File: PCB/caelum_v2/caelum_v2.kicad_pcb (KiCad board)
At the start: 2 copper layers, 69 x 40.5 mm, 36 parts, among them J1 SS445P, J2 i2C Bus2, J3 Pulse1, J4 Batt, J7 I2C BUS1, J8 DS18B20, Q1 FS8205A-FC, U1 DW01A, U2 MCP1825S, U3 ESP32-H2-SUPERMINI

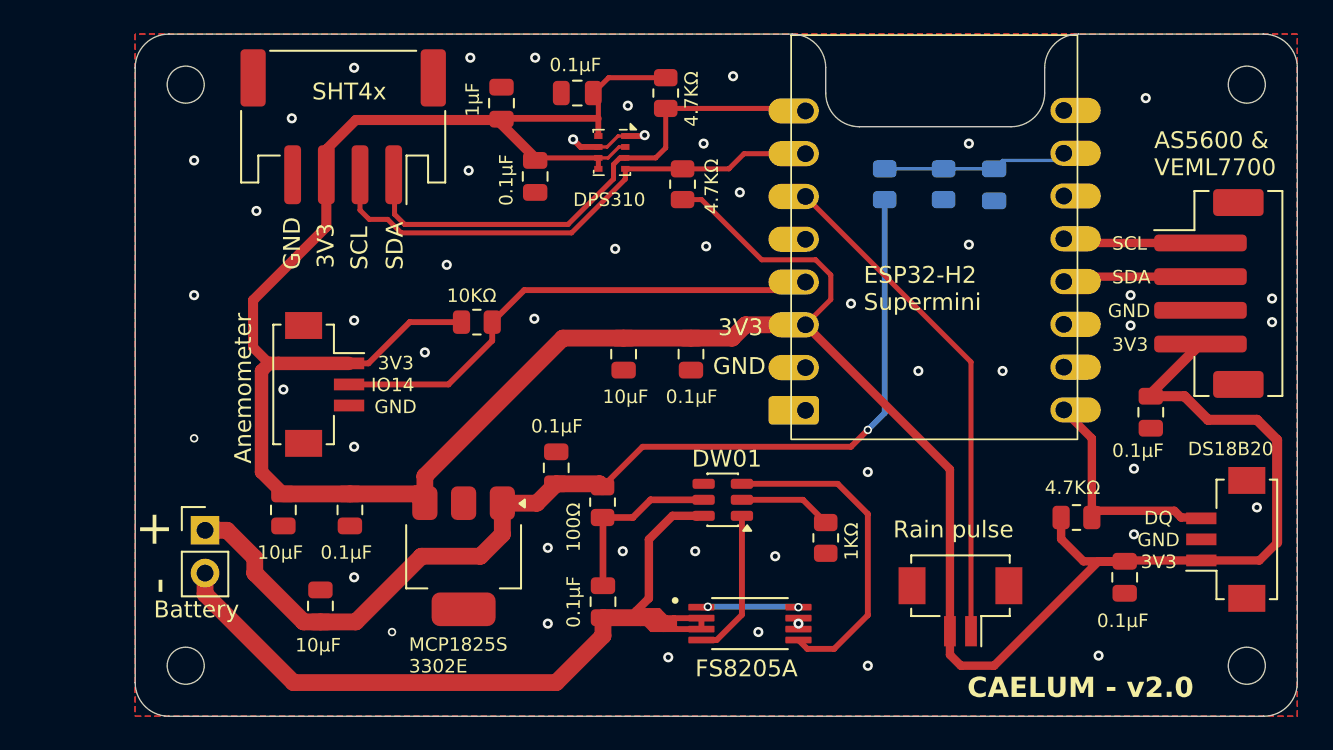
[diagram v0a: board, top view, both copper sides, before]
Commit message: Clone of Caelum v1
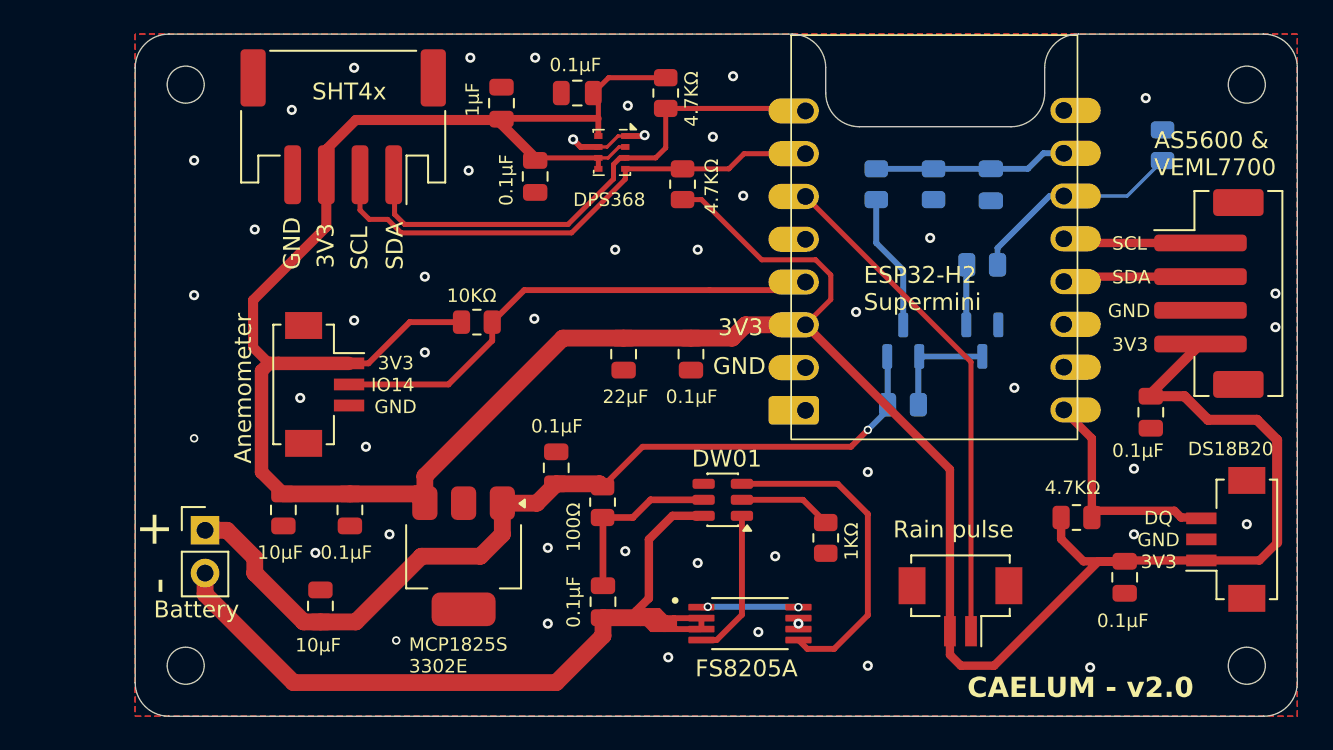
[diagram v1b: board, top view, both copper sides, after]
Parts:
- added Q2: BSS138, Package_TO_SOT_SMD:SOT-23, B.Cu at (96.3, 43.7)
- added Q3: Si2323DS, Package_TO_SOT_SMD:SOT-23, B.Cu at (91.6, 43.7)
- added R10: 100K, Resistor_SMD:R_0805_2012Metric, B.Cu at (107.0, 32.1)
- added R11: 100, Resistor_SMD:R_0805_2012Metric, B.Cu at (96.3, 39.2)
- added R9: 100K, Resistor_SMD:R_0805_2012Metric, B.Cu at (91.6, 47.5)
- R4: value 100K -> 10K
- R5: value 100K -> 22K
- moved R5 0.60 mm to (93.4, 34.4)
- moved R4 0.50 mm to (90.0, 34.4)
- moved C9 0.20 mm to (96.8, 34.5)
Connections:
- R4 pad 2: BATT+ -> Net-(Q3-D)
- U3 pad 14: unconnected-(U3-IO3-Pad14) -> GPIO3
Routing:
- net GPIO3: track 0.00 -> 12.9 mm
- net BATT+: track 62.2 -> 52.9 mm
- net Net-(Q3-D): track 0.00 -> 8.11 mm
- net Net-(Q2-D): track 0.00 -> 6.60 mm
- net Net-(Q2-G): track 0.00 -> 3.57 mm
- net GPIO4: track 11.0 -> 12.1 mm
- net OUT-: vias 49 -> 46
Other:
- board text added: "220KΩ"
- board text added: "22KΩ"
- board text added: "22µF"
- board text added: "BSS138"
- board text added: "DPS368"
- board text added: "Si2323"
- board text removed: "DPS310"

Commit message: Add ESP32 symbol and wind vane macro; update library paths
- Updated the library path for "caelum_v2" in fp-lib-table.
- Added ESP32 symbol to sym-lib-table for better component management.
- Created a new FreeCAD macro for generating a wind vane assembly compatible with the AS5600 sensor, including detailed parameters and assembly instructions.
- Introduced various components such as the rotating shaft, magnet holder, wind vane, arrow pointer, counterweight, central body, base mount, and sensor mount area.
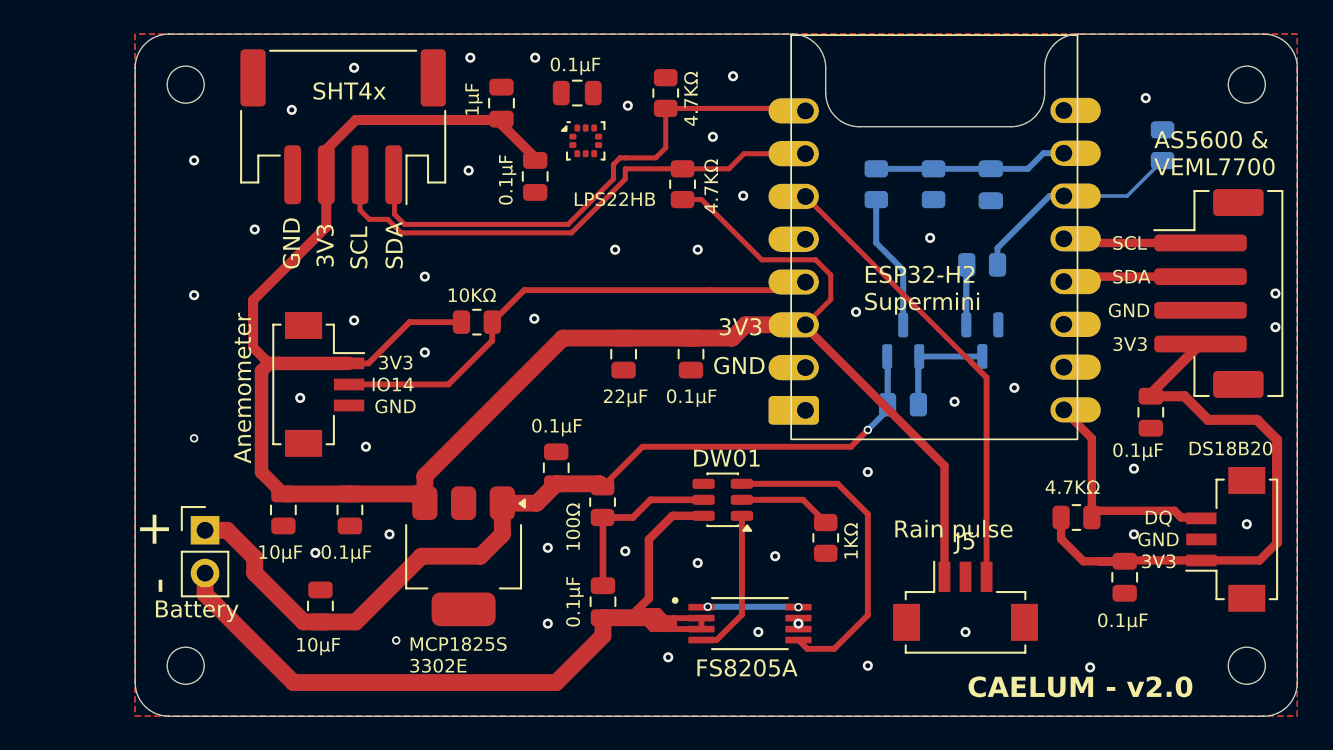
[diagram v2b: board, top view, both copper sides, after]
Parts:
- removed J3: Pulse1, Connector_Hirose:Hirose_DF13C_CL535-0402-2-51_1x02-1MP_P1.25mm_Vertical
- removed U4: ~, Package_LGA:Bosch_LGA-8_2x2.5mm_P0.65mm_ClockwisePinNumbering
- added J5: DRV5032DULPG(M), Connector_Hirose:Hirose_DF13C_CL535-0403-5-51_1x03-1MP_P1.25mm_Vertical, F.Cu at (95.3, 59.2)
- added U5: LPS22HB, Package_LGA:ST_HLGA-10_2x2mm_P0.5mm_LayoutBorder3x2y, F.Cu at (72.8, 31.8)
- C6: value 10µF -> 22µF
- R10: value 100K -> 220K-470K
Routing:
- net +3V3: track 191.1 -> 155.1 mm
- net OUT-: track 5.30 -> 0.57 mm
- net GPIO12: track 29.9 -> 27.0 mm
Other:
- board text added: "LPS22HB"
- board text removed: "DPS368"

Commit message: Refactor code structure for improved readability and maintainability
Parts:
- removed C12: 0.1µF, Capacitor_SMD:C_0805_2012Metric
- J1, J5, J8: footprint Connector_Hirose:Hirose_DF13C_CL535-0403-5-51_1x03-1MP_P1.25mm_Vertical -> Connector_JST:JST_PH_B3B-PH-SM4-TB_1x03-1MP_P2.00mm_Vertical
- J2: footprint Connector_JST:JST_PH_B4B-PH-SM4-TB_1x04-1MP_P2.00mm_Vertical -> Connector_JST:JST_PH_S4B-PH-SM4-TB_1x04-1MP_P2.00mm_Horizontal
- J4: footprint Connector_PinHeader_2.54mm:PinHeader_1x02_P2.54mm_Vertical -> Connector_JST:JST_PH_S2B-PH-SM4-TB_1x02-1MP_P2.00mm_Horizontal
- moved R8 6.03 mm to (71.7, 40.0)
- moved H1 6.00 mm to (43.0, 28.5)
- moved H2 6.00 mm to (43.0, 63.0)
- moved U5 5.67 mm to (75.2, 37.0)
- moved J4 5.35 mm to (45.0, 53.5), turned to 180 degrees
- moved J1 4.40 mm to (61.5, 45.0), turned to 90 degrees
- moved C10 3.56 mm to (72.0, 32.5), turned to 90 degrees
- moved C11 3.15 mm to (68.7, 32.6), turned to 90 degrees
- moved J2 1.91 mm to (109.5, 39.0), turned to 90 degrees
- moved J8 1.54 mm to (109.7, 54.4), turned to -90 degrees
- moved J5 0.22 mm to (95.5, 59.0), turned to 180 degrees
- moved J7 0.10 mm to (58.4, 31.1)
- turned C13 to 90 degrees
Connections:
- C13 pad 1: +3V3 -> OUT-
- C13 pad 2: OUT- -> +3V3
- J1 pad 1: +3V3 -> GPIO14
- J1 pad 2: GPIO14 -> OUT-
- J1 pad 3: OUT- -> +3V3
- J1 pad MP: (no net) -> OUT-
- J2 pad 1: SCL_2 -> OUT-
- J2 pad 2: SDA_2 -> +3V3
- J2 pad 3: OUT- -> SDA_2
- J2 pad 4: +3V3 -> SCL_2
- J2 pad MP: (no net) -> OUT-
- J5 pad 1: +3V3 -> GPIO13
- J5 pad 3: GPIO12 -> +3V3
- J5 pad MP: (no net) -> OUT-
- J7 pad 1: SDA -> OUT-
- J7 pad 2: SCL -> +3V3
- J7 pad 3: +3V3 -> SDA
- J7 pad 4: OUT- -> SCL
- J7 pad MP: (no net) -> OUT-
- J8 pad 1: +3V3 -> GPIO24
- J8 pad 3: GPIO24 -> +3V3
- J8 pad MP: (no net) -> OUT-
- U3 pad 5: unconnected-(U3-IO13-Pad5) -> GPIO13
- U5 pad 1: unconnected-(U5-Vdd_IO-Pad1) -> +3V3
- U5 pad 10: unconnected-(U5-VDD-Pad10) -> +3V3
- U5 pad 2: unconnected-(U5-SCL-Pad2) -> SCL
- U5 pad 3: Net-(U5-GND-Pad3) -> OUT-
- U5 pad 4: unconnected-(U5-SDA-Pad4) -> SDA
- U5 pad 5: unconnected-(U5-SA0-Pad5) -> +3V3
- U5 pad 6: unconnected-(U5-~{CS}-Pad6) -> +3V3
- U5 pad 7: unconnected-(U5-INT_DRDY-Pad7) -> GPIO12
- U5 pad 8: Net-(U5-GND-Pad3) -> OUT-
- U5 pad 9: Net-(U5-GND-Pad3) -> OUT-
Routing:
- net +3V3: track 155.1 -> 210.9 mm, vias 0 -> 2
- net GPIO13: track 0.00 -> 27.6 mm
- net GPIO12: track 27.0 -> 11.7 mm, vias 0 -> 1
- net SDA: track 31.1 -> 40.9 mm, vias 0 -> 2
- net BATT-: track 56.2 -> 63.2 mm
- net SCL: track 31.4 -> 37.7 mm
- net BATT+: track 52.9 -> 56.0 mm
- net OUT-: track 0.57 -> 3.49 mm, vias 46 -> 50
- net GPIO14: track 30.3 -> 27.9 mm
- net SCL_2: track 8.22 -> 6.57 mm
- net unconnected-(U3-IO13-Pad5): track 1.43 -> 0.00 mm
- net SDA_2: track 8.24 -> 6.86 mm
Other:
- board size 69 x 40.5 mm -> 75 x 40.5 mm
- board text added: "IO12"
- board text removed: "CAELUM - v2.0"

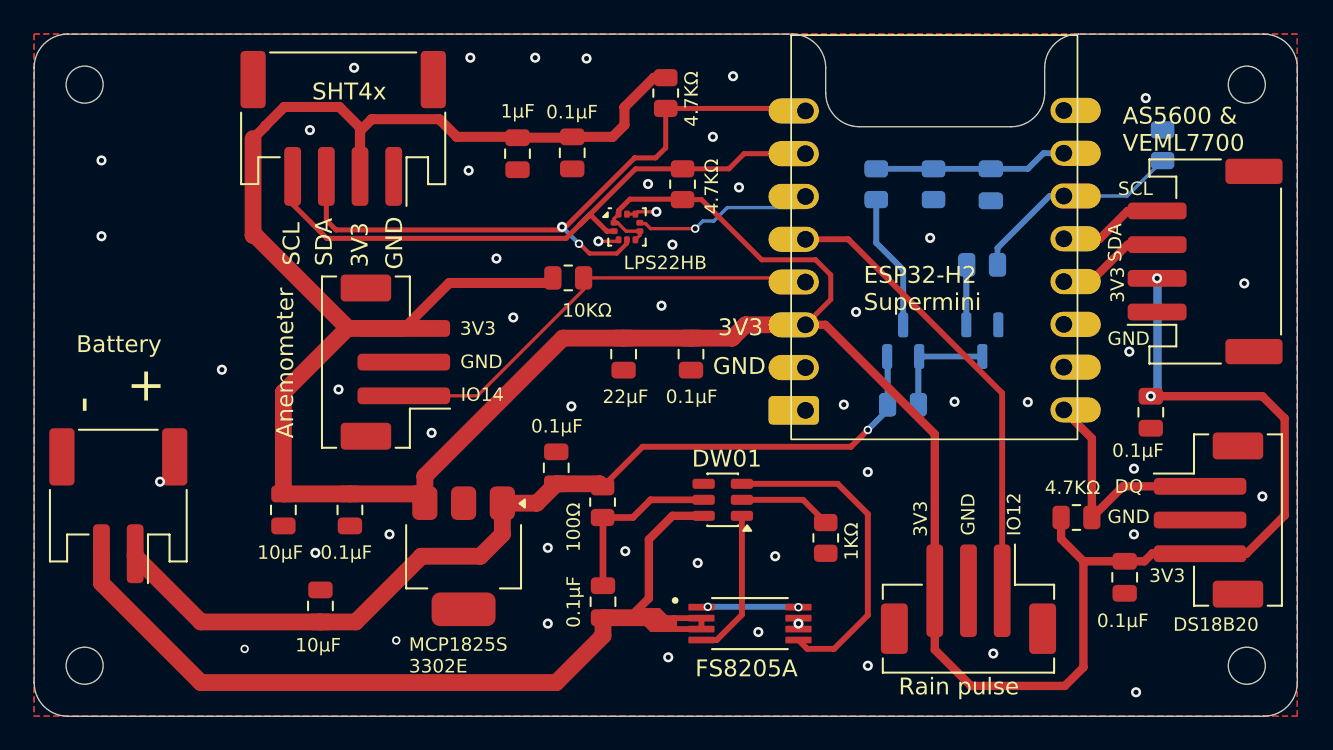
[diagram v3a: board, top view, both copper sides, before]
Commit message: Update PCB settings: change active layer to 0 and adjust pad dimensions
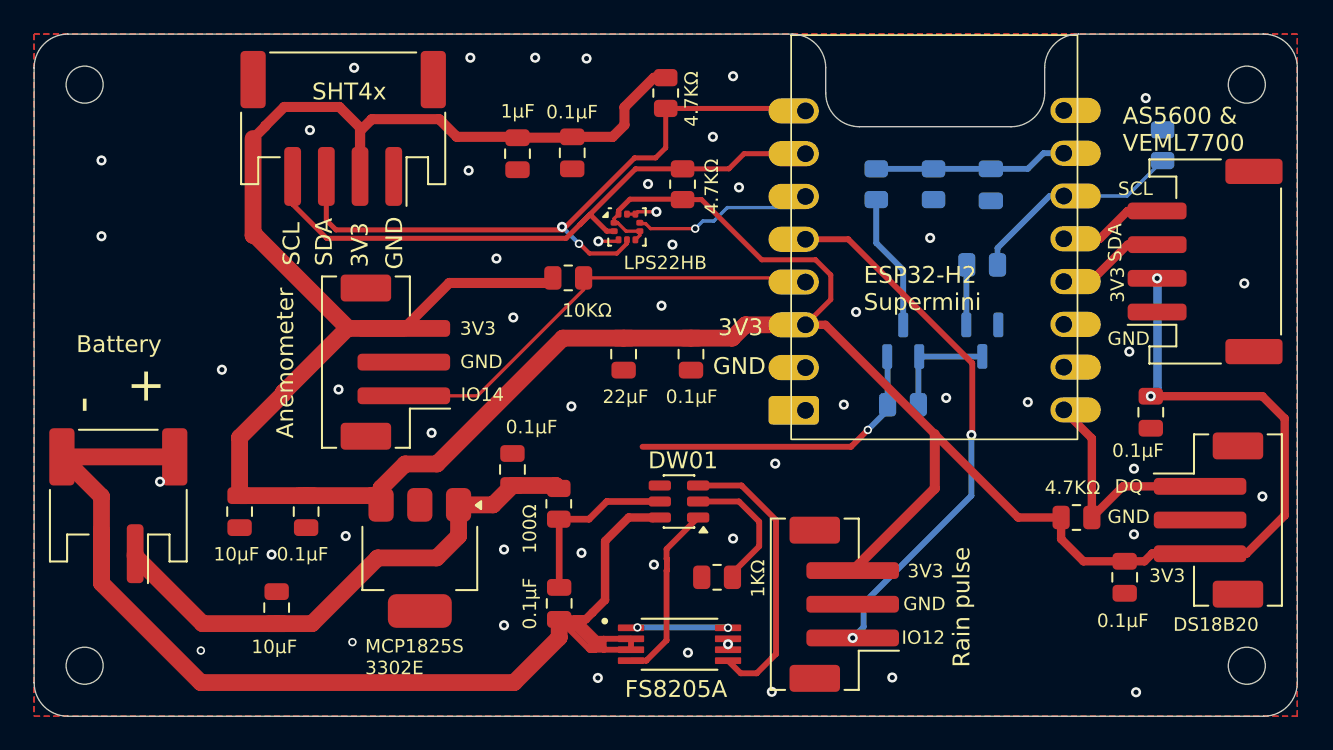
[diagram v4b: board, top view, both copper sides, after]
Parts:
- moved J5 7.38 mm to (88.1, 59.4), turned to 90 degrees
- moved R2 6.86 mm to (80.5, 57.8), turned to 180 degrees
- moved Q1 4.36 mm to (78.3, 61.7)
- moved C1 2.60 mm to (71.2, 59.3)
- moved U1 2.60 mm to (78.3, 53.2)
- moved C2 2.60 mm to (54.4, 59.5)
- moved C5 2.60 mm to (56.1, 53.9)
- moved U2 2.60 mm to (62.9, 56.6)
- moved C3 2.60 mm to (68.4, 51.4)
- moved C4 2.60 mm to (52.2, 53.9)
- moved R1 2.60 mm to (71.2, 53.4)
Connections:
- J1 pad MP: OUT- -> (no net)
- J2 pad MP: OUT- -> (no net)
- J4 pad MP: OUT- -> BATT-
- J7 pad MP: OUT- -> (no net)
- J8 pad MP: OUT- -> (no net)
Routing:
- net BATT-: track 63.2 -> 72.9 mm
- net +3V3: track 210.9 -> 204.8 mm
- net BATT+: track 56.0 -> 50.1 mm
- net GPIO13: track 27.6 -> 32.7 mm, vias 0 -> 2
- net Net-(U1-CS): track 5.53 -> 8.18 mm
- net Net-(Q1-G2): track 19.4 -> 17.1 mm
- net Net-(Q1-G1): track 8.90 -> 10.7 mm
